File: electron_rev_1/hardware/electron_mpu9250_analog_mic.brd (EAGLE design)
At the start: 22.2 x 102.8 mm, 42 parts, among them IC2 S25FL128SAGNFI011, IC4 MIC_I2S_SPH0645, U1 MPU-9250, U10 GAS_SENSOR, U2 Value, U3 OPA322AIDBVT, U4 microSD, U5 +12v, U6 +12v, U7 GAS_SENSOR

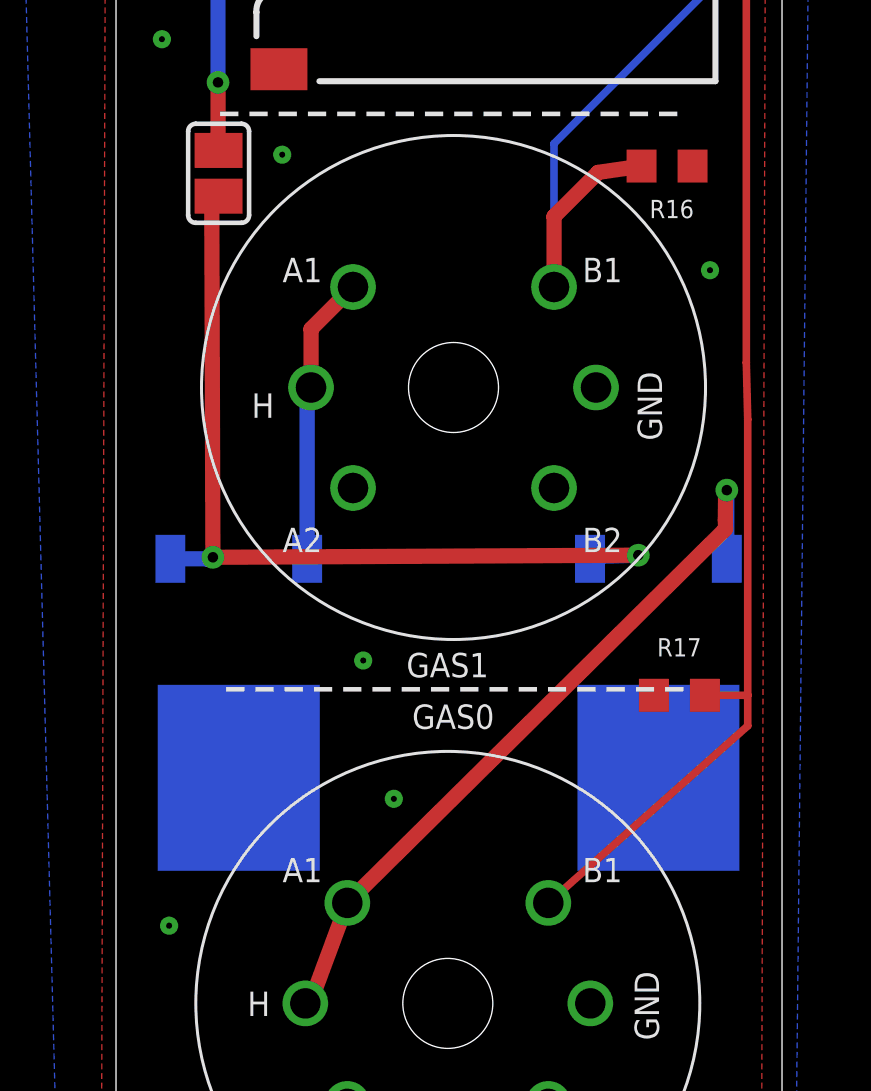
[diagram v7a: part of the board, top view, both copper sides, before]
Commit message: seperate solder jumpers for gas sensors
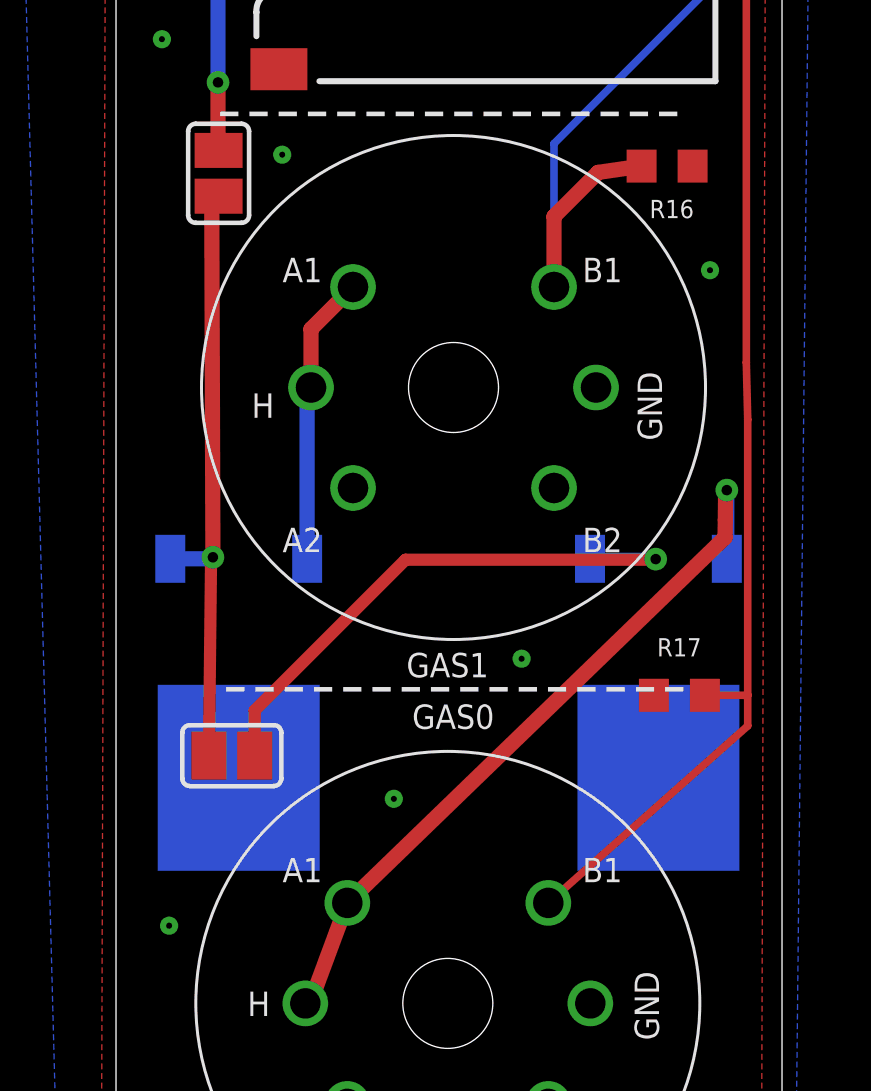
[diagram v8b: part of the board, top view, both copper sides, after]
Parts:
- added SJ2: (no value), jumper:SJ
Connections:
- removed net N$10: SJ1.1, U5.1, U6.1
- new net N$11: SJ2.1, U6.1
- net VBAT: now also SJ1.1, SJ2.2, U5.1
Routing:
- net N$10: track 30.1 -> 0.00 mm, vias 2 -> 0
- net VBAT: track 24.8 -> 45.6 mm, vias 1 -> 2
- net N$11: track 0.00 -> 19.2 mm, vias 0 -> 1
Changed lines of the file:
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@@
 <attribute name="VALUE" x="2.87" y="-17.9699" size="0.02" layer="27" rot="R90"/>
+</element>
+<element name="SJ2" library="jumper" library_urn="urn:adsk.eagle:library:252" package="SJ" package3d_urn="urn:adsk.eagle:package:15471/1" value="" x="3.31" y="-37.78" smashed="yes" rot="R180">
+<attribute name="VALUE" x="2.9099" y="-37.78" size="0.02" layer="27" rot="R180"/>
 </element>
 </elements>
@@
 <via x="4.99" y="-17.75" extent="1-16" drill="0.2"/>
 <via x="19.25" y="-21.6" extent="1-16" drill="0.2"/>
-<via x="7.69" y="-34.61" extent="1-16" drill="0.2"/>
+<via x="12.97" y="-34.55" extent="1-16" drill="0.2"/>
 <via x="8.71" y="-39.22" extent="1-16" drill="0.2"/>
 <via x="1.22" y="-43.45" extent="1-16" drill="0.2"/>
@@
 <wire x1="2.85" y1="-15.34" x2="2.85" y2="-17.108" width="0.508" layer="1"/>
 <wire x1="2.85" y1="-17.108" x2="2.87" y2="-17.608" width="0.508" layer="1"/>
+<contactref element="SJ2" pad="2"/>
+<contactref element="U5" pad="1"/>
+<contactref element="SJ1" pad="1"/>
+<wire x1="1.26" y1="-31.22" x2="2.51" y2="-31.22" width="0.508" layer="16"/>
+<wire x1="2.51" y1="-31.22" x2="2.54" y2="-31.25" width="0.508" layer="16"/>
+<wire x1="2.54" y1="-31.25" x2="2.6" y2="-31.25" width="0.508" layer="16"/>
+<wire x1="2.6" y1="-31.25" x2="2.68" y2="-31.17" width="0.508" layer="16"/>
+<via x="2.68" y="-31.17" extent="1-16" drill="0.35"/>
+<wire x1="2.68" y1="-31.17" x2="2.64" y2="-18.8472" width="0.508" layer="1"/>
+<wire x1="2.87" y1="-19.132" x2="2.87" y2="-19.0772" width="0.4064" layer="1"/>
+<wire x1="2.87" y1="-19.0772" x2="2.64" y2="-18.8472" width="0.4064" layer="1"/>
+<wire x1="2.548" y1="-37.78" x2="2.618" y2="-31.232" width="0.4064" layer="1"/>
+<wire x1="2.618" y1="-31.232" x2="2.68" y2="-31.17" width="0.4064" layer="1"/>
+<wire x1="2.87" y1="-17.608" x2="2.64" y2="-18.8472" width="0" layer="19" extent="1-1"/>
 </signal>
 <signal name="D7">
@@
 <wire x1="19.77" y1="-29.02" x2="19.81" y2="-28.93" width="0.508" layer="1"/>
 <contactref element="U7" pad="A1"/>
-<wire x1="19.77" y1="-30.22" x2="7.16" y2="-42.69" width="0.508" layer="1"/>
-<wire x1="19.77" y1="-30.22" x2="19.76" y2="-29.93" width="0.508" layer="1"/>
+<wire x1="19.75" y1="-30.51" x2="7.16" y2="-42.69" width="0.508" layer="1"/>
+<wire x1="19.75" y1="-30.51" x2="19.76" y2="-29.93" width="0.508" layer="1"/>
 <wire x1="7.16" y1="-42.69" x2="5.91" y2="-46.06" width="0.508" layer="1"/>
 </signal>
@@
 <wire x1="11.66" y1="2.69" x2="10.96" y2="2.69" width="0.254" layer="1"/>
 </signal>
-<signal name="N$10">
+<signal name="N$11">
 <contactref element="U6" pad="1"/>
-<contactref element="U5" pad="1"/>
-<wire x1="1.26" y1="-31.22" x2="2.51" y2="-31.22" width="0.508" layer="16"/>
-<wire x1="2.51" y1="-31.22" x2="2.54" y2="-31.25" width="0.508" layer="16"/>
-<wire x1="2.54" y1="-31.25" x2="2.6" y2="-31.25" width="0.508" layer="16"/>
-<wire x1="2.6" y1="-31.25" x2="2.68" y2="-31.17" width="0.508" layer="16"/>
-<via x="2.68" y="-31.17" extent="1-16" drill="0.35"/>
-<wire x1="2.68" y1="-31.17" x2="16.73" y2="-31.1" width="0.508" layer="1"/>
-<wire x1="16.73" y1="-31.1" x2="16.86" y2="-31.1" width="0.508" layer="1"/>
-<wire x1="16.76" y1="-31.06" x2="16.86" y2="-31.1" width="0.508" layer="1"/>
-<via x="16.86" y="-31.1" extent="1-16" drill="0.35"/>
-<wire x1="16.86" y1="-31.1" x2="15.33" y2="-31.14" width="0.508" layer="16"/>
-<wire x1="15.33" y1="-31.14" x2="15.25" y2="-31.22" width="0.508" layer="16"/>
-<wire x1="2.64" y1="-18.8472" x2="2.68" y2="-31.17" width="0.508" layer="1"/>
-<contactref element="SJ1" pad="1"/>
-<wire x1="2.87" y1="-19.132" x2="2.87" y2="-19.0772" width="0.4064" layer="1"/>
-<wire x1="2.87" y1="-19.0772" x2="2.64" y2="-18.8472" width="0.4064" layer="1"/>
+<contactref element="SJ2" pad="1"/>
+<wire x1="15.25" y1="-31.22" x2="17.43" y2="-31.22" width="0.4064" layer="16"/>
+<wire x1="17.43" y1="-31.22" x2="17.44" y2="-31.23" width="0.4064" layer="16"/>
+<wire x1="17.45" y1="-31.24" x2="17.44" y2="-31.23" width="0.4064" layer="16"/>
+<via x="17.44" y="-31.23" extent="1-16" drill="0.35"/>
+<wire x1="17.44" y1="-31.23" x2="17.42" y2="-31.21" width="0.4064" layer="1"/>
+<wire x1="4.072" y1="-37.78" x2="4.072" y2="-36.278" width="0.4064" layer="1"/>
+<wire x1="4.072" y1="-36.278" x2="9.1" y2="-31.25" width="0.4064" layer="1"/>
+<wire x1="9.1" y1="-31.25" x2="17.42" y2="-31.25" width="0.4064" layer="1"/>
+<wire x1="17.42" y1="-31.25" x2="17.44" y2="-31.23" width="0.4064" layer="1"/>
 </signal>
 </signals>
